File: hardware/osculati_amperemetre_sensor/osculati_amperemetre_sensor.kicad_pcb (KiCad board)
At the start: 2 copper layers, 50 x 40 mm, 28 parts, among them J1 Screw_Terminal_01x02, J2 Screw_Terminal_01x02, J3 Screw_Terminal_01x03, U1 LM4040DBZ-2.0, U2 MCP6007-xSN, U3 INA186A2, U4 LDL1117S50

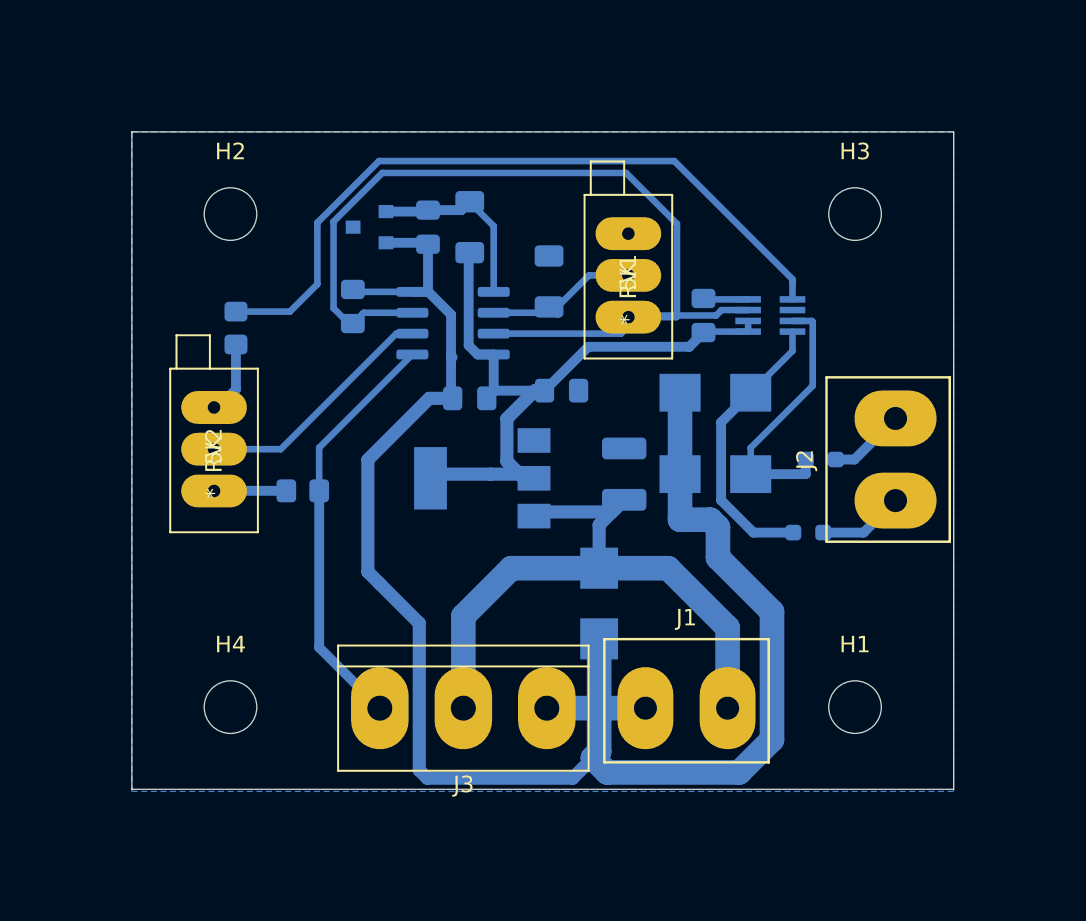
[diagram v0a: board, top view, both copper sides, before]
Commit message: Add a 6mm margin around PCB.
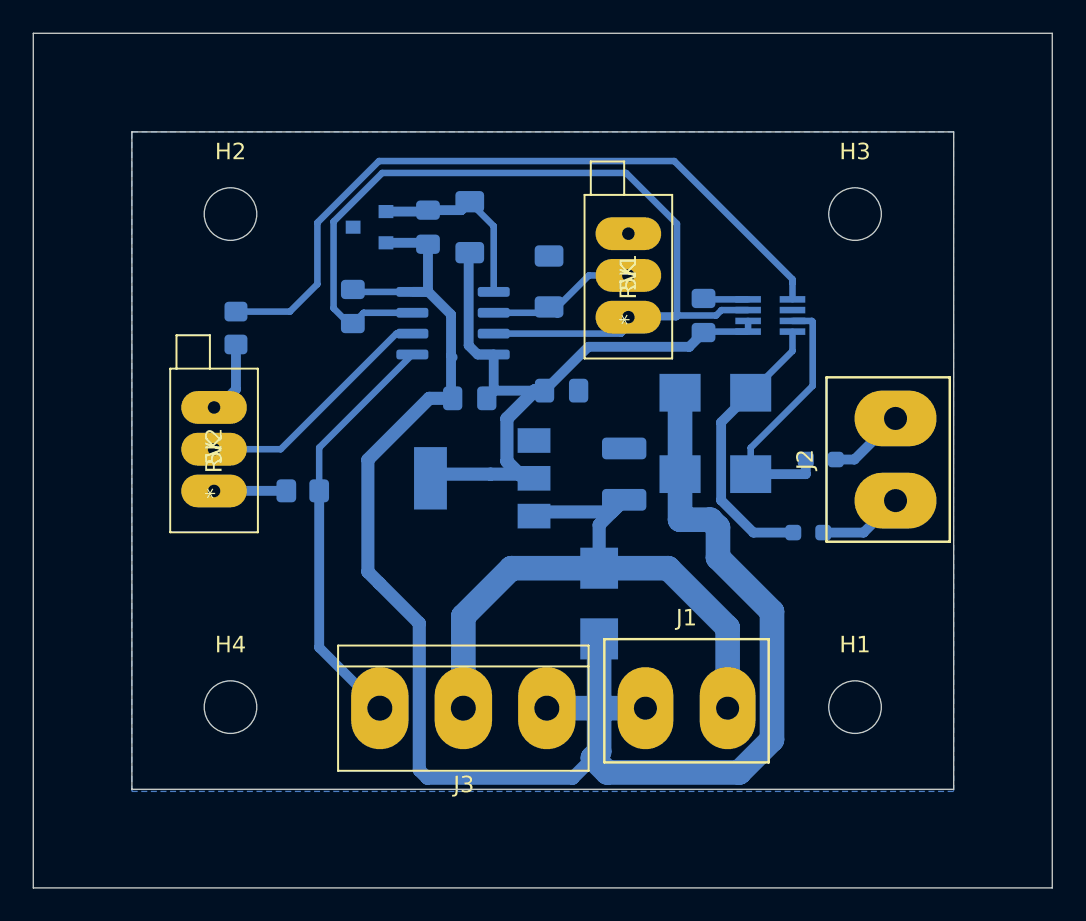
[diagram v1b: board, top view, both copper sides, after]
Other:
- board size 50 x 40 mm -> 62 x 52 mm
